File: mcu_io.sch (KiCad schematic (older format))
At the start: 6 parts

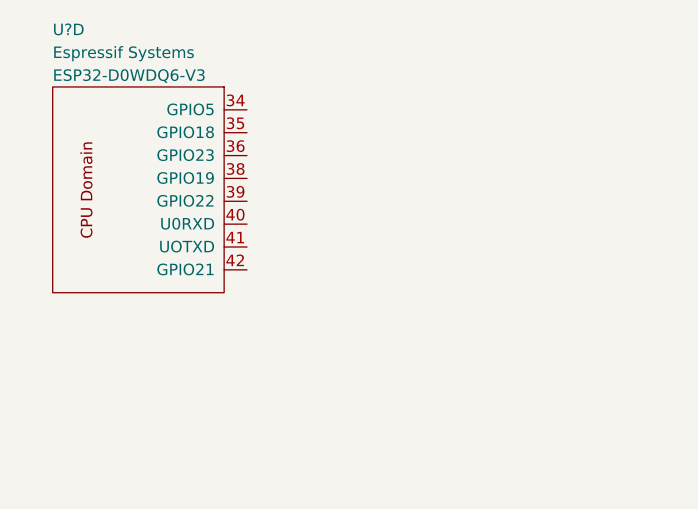
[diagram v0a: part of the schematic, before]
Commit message: Add power and boot mode LED's.
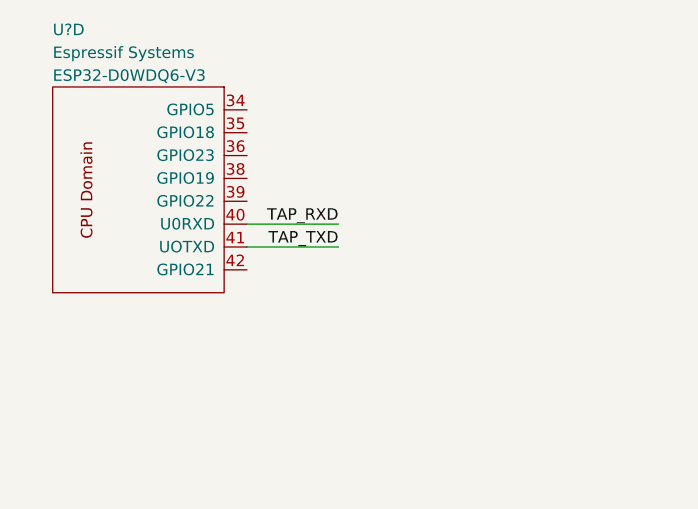
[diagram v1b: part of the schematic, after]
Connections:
- net TAP_RXD: now reaches U?.40 (U0RXD)
- net TAP_TXD: now reaches U?.41 (UOTXD)
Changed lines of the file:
@@
 	0    1    1    0
 $EndComp
+Wire Wire Line
+	2150 1900 2550 1900
+Wire Wire Line
+	2150 2000 2550 2000
+Text Label 2550 2000 2    50   ~ 0
+TAP_TXD
+Text Label 2550 1900 2    50   ~ 0
+TAP_RXD
 $EndSCHEMATC

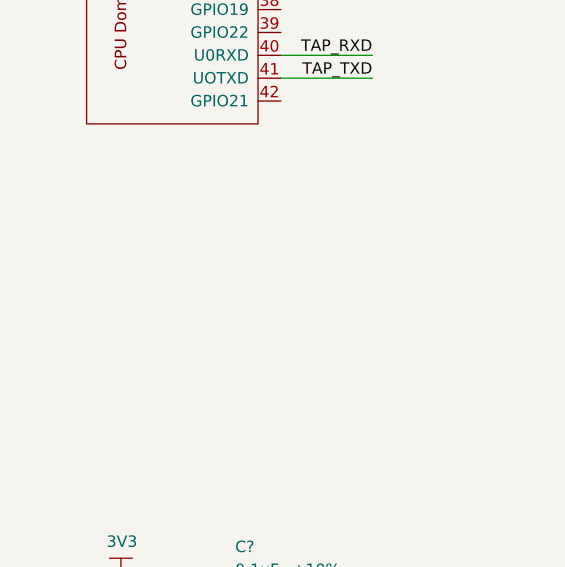
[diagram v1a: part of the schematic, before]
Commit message: Add TAP interface.
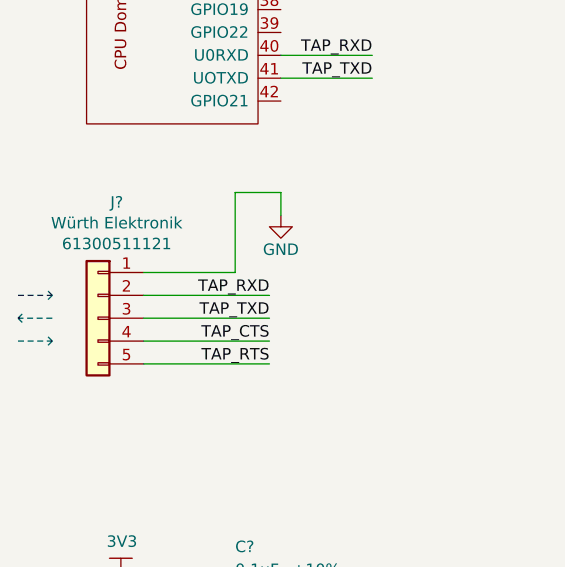
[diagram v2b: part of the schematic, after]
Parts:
- added J?: WE-61300511121, footprints:WE-61300511121_HDRV5W79P254_5X1_1270X254H854, symbol gz_Rectangular-Connectors-Headers-Male-Pins:WE-61300511121
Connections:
- net GND: now also J?.1 (Pin_1)
- net TAP_RXD: now also J?.2 (Pin_2)
- net TAP_TXD: now also J?.3 (Pin_3)
- new net TAP_CTS: J?.4 (Pin_4)
- new net TAP_RTS: J?.5 (Pin_5)
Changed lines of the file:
@@
 Text Label 2550 1900 2    50   ~ 0
 TAP_RXD
+$Comp
+L gz_Rectangular-Connectors-Headers-Male-Pins:WE-61300511121 J?
+U 1 1 604FF7D2
+P 1350 3050
+F 0 "J?" H 1432 3557 50  0000 C CNN
+F 1 "WE-61300511121" H 1850 3900 50  0001 L CNN
+F 2 "footprints:WE-61300511121_HDRV5W79P254_5X1_1270X254H854" H 1850 4000 50  0001 L CNN
+F 3 "${DATASHEETS}/WE-6130xx11121.pdf" H 2150 2900 50  0001 L CNN
+F 4 "Digikey" H 1850 3800 50  0001 L CNN "Vendor"
+F 5 "732-5318-ND" H 2150 3800 50  0001 L CNN "Vendor_PN"
+F 6 "Würth Elektronik" H 1432 3466 50  0000 C CNN "Manufacturer"
+F 7 "61300511121" H 1432 3375 50  0000 C CNN "MPN"
+F 8 "Connectors, Interconnects" H 1850 3700 50  0001 L CNN "Category"
+F 9 "Rectangular Connectors - Headers, Male Pins" H 1850 3600 50  0001 L CNN "Family"
+F 10 "Yes" H 1350 3400 50  0001 L CNN "Fit"
+	1    1350 3050
+	1    0    0    -1
+$EndComp
+Wire Wire Line
+	1550 2850 1950 2850
+Wire Wire Line
+	1550 2950 2100 2950
+Wire Wire Line
+	1550 3050 2100 3050
+Wire Wire Line
+	1550 3150 2100 3150
+Wire Wire Line
+	1550 3250 2100 3250
+$Comp
+L gz_Power-Symbols:GND #PWR?
+U 1 1 605045A7
+P 2150 2600
+AR Path="/60330427/605045A7" Ref="#PWR?"  Part="1"
+AR Path="/606CDE66/605045A7" Ref="#PWR?"  Part="1"
+F 0 "#PWR?" H 2150 2350 50  0001 C CNN
+F 1 "GND" H 2150 2450 50  0000 C CNN
+F 2 "" H 2150 2600 50  0001 C CNN
+F 3 "" H 2150 2600 50  0001 C CNN
+	1    2150 2600
+	1    0    0    -1
+$EndComp
+Wire Wire Line
+	2150 2600 2150 2500
+Wire Wire Line
+	2150 2500 1950 2500
+Wire Wire Line
+	1950 2500 1950 2850
+Text Label 2100 2950 2    50   ~ 0
+TAP_RXD
+Text Label 2100 3050 2    50   ~ 0
+TAP_TXD
+Text Label 2100 3150 2    50   ~ 0
+TAP_CTS
+Text Label 2100 3250 2    50   ~ 0
+TAP_RTS
+Wire Notes Line style solid
+	1000 2950 1150 2950
+Wire Notes Line style solid
+	1150 2950 1125 2925
+Wire Notes Line style solid
+	1150 2950 1125 2975
+Wire Notes Line style solid
+	1150 3050 1000 3050
+Wire Notes Line style solid
+	1000 3050 1025 3075
+Wire Notes Line style solid
+	1000 3050 1025 3025
+Wire Notes Line style solid
+	1000 3150 1150 3150
+Wire Notes Line style solid
+	1150 3150 1125 3125
+Wire Notes Line style solid
+	1150 3150 1125 3175
 $EndSCHEMATC

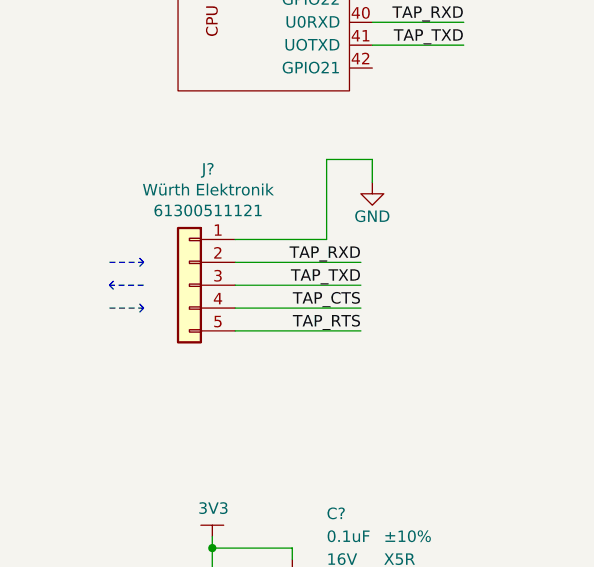
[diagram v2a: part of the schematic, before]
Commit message: Add flow control to TAP to auto-flash ESP32.
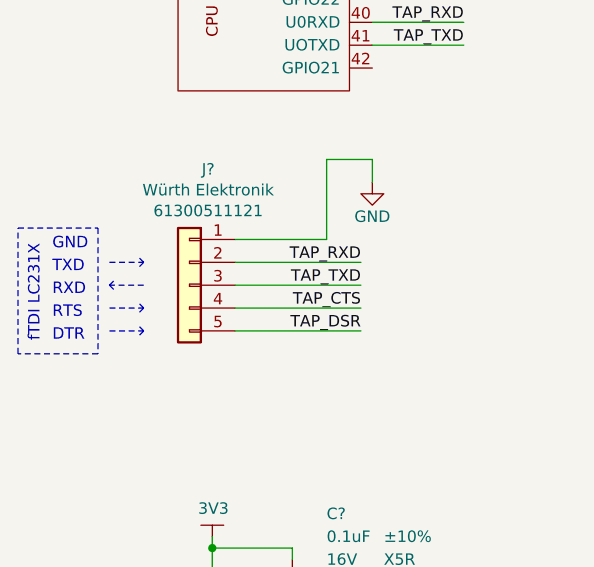
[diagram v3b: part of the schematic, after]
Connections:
- net TAP_RTS renamed TAP_DSR
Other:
- note added: "DTR"
- note added: "GND"
- note added: "RTS"
- note added: "RXD"
- note added: "TXD"
- note added: "fTDI LC231X"
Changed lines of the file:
@@
 TAP_CTS
 Text Label 2100 3250 2    50   ~ 0
-TAP_RTS
+TAP_DSR
 Wire Notes Line style solid
 	1000 2950 1150 2950
@@
 Wire Notes Line style solid
 	1150 3150 1125 3175
+Wire Notes Line style solid
+	1000 3250 1150 3250
+Wire Notes Line style solid
+	1150 3250 1125 3225
+Wire Notes Line style solid
+	1150 3250 1125 3275
+Text Notes 750  3000 0    50   ~ 0
+TXD
+Text Notes 750  3100 0    50   ~ 0
+RXD
+Text Notes 750  3200 0    50   ~ 0
+RTS
+Text Notes 750  3300 0    50   ~ 0
+DTR
+Text Notes 750  2900 0    50   ~ 0
+GND
+Text Notes 700  3300 1    50   ~ 0
+fTDI LC231X
+Wire Notes Line
+	600  2800 950  2800
+Wire Notes Line
+	950  2800 950  3350
+Wire Notes Line
+	950  3350 600  3350
+Wire Notes Line
+	600  3350 600  2800
 $EndSCHEMATC

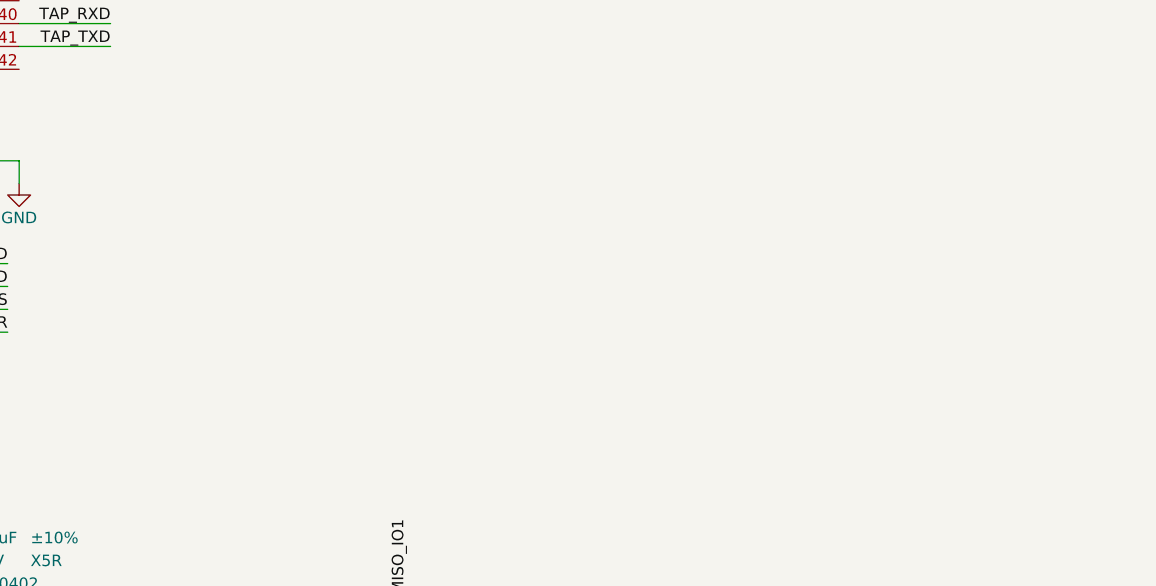
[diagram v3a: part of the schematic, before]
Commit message: Add auto-flash circuit to prevent DTR == 1 && RTS == 1 condition to keep ESP32 in reset.
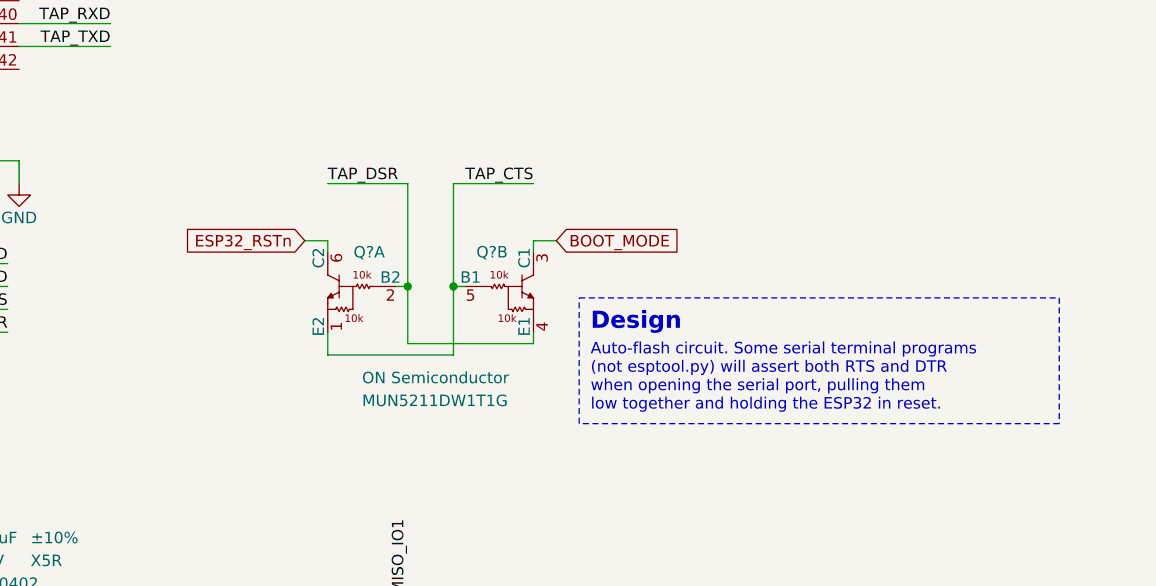
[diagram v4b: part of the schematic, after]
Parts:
- added Q? (x2): ON-Semi_MUN5211DW1T1G, footprints:ON-Semi-MUN5211DW1T1G_SOT23-6P65_210X110L36X20L, symbol gz_Transistors-Bipolar-BJT-Arrays-Pre-Biased:ON-Semi_MUN5211DW1T1G
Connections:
- net TAP_CTS: now also Q?.1 (E2), Q?.5 (B1)
- net TAP_DSR: now also Q?.2 (B2), Q?.4 (E1)
- new net BOOT_MODE: Q?.3 (C1)
- new net ESP32_RSTn: Q?.6 (C2)
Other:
- note added: "Auto-flash circuit. Some serial terminal programs\n(not esptool.py) will assert both RTS and DTR \nwhen opening the serial port, pulling them\nlow together and holding the ESP32 in reset."
- note added: "Design"
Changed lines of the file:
@@
 Text Notes 700  3300 1    50   ~ 0
 fTDI LC231X
+Wire Notes Line style solid
+	600  2800 950  2800
+Wire Notes Line style solid
+	950  2800 950  3350
+Wire Notes Line style solid
+	950  3350 600  3350
+Wire Notes Line style solid
+	600  3350 600  2800
+$Comp
+L gz_Transistors-Bipolar-BJT-Arrays-Pre-Biased:ON-Semi_MUN5211DW1T1G Q?
+U 1 1 6050B898
+P 3550 3050
+F 0 "Q?" H 3350 3200 50  0000 L CNN
+F 1 "ON-Semi_MUN5211DW1T1G" H 3900 4500 50  0001 L CNN
+F 2 "footprints:ON-Semi-MUN5211DW1T1G_SOT23-6P65_210X110L36X20L" H 3900 4600 50  0001 L CNN
+F 3 "${DATASHEETS}/ON-Semi_MUN5211DW1T1G.pdf" H 3900 3500 50  0001 L CNN
+F 4 "Digikey" H 3900 4400 50  0001 L CNN "Vendor"
+F 5 "MUN5211DW1T1GOSCT-ND" H 4300 4400 50  0001 L CNN "Vendor_PN"
+F 6 "ON Semiconductor" H 3700 3000 50  0001 L CNN "Manufacturer"
+F 7 "MUN5211DW1T1G" H 3750 2900 50  0001 L CNN "MPN"
+F 8 "Discrete Semiconductor Products" H 3900 4300 50  0001 L CNN "Category"
+F 9 "Transistors - Bipolar (BJT) - Arrays, Pre-Biased" H 5300 4300 50  0001 L CNN "Family"
+F 10 "Yes" H 3850 3050 50  0001 L CNN "Fit"
+F 11 "SOT-363" H 3900 4200 50  0001 L CNN "Package"
+	1    3550 3050
+	-1   0    0    -1
+$EndComp
+$Comp
+L gz_Transistors-Bipolar-BJT-Arrays-Pre-Biased:ON-Semi_MUN5211DW1T1G Q?
+U 2 1 6050C9A5
+P 4350 3050
+F 0 "Q?" H 4150 3200 50  0000 L CNN
+F 1 "ON-Semi_MUN5211DW1T1G" H 4700 4500 50  0001 L CNN
+F 2 "footprints:ON-Semi-MUN5211DW1T1G_SOT23-6P65_210X110L36X20L" H 4700 4600 50  0001 L CNN
+F 3 "${DATASHEETS}/ON-Semi_MUN5211DW1T1G.pdf" H 4700 3500 50  0001 L CNN
+F 4 "Digikey" H 4700 4400 50  0001 L CNN "Vendor"
+F 5 "MUN5211DW1T1GOSCT-ND" H 5100 4400 50  0001 L CNN "Vendor_PN"
+F 6 "ON Semiconductor" H 3650 2650 50  0000 L CNN "Manufacturer"
+F 7 "MUN5211DW1T1G" H 3650 2550 50  0000 L CNN "MPN"
+F 8 "Discrete Semiconductor Products" H 4700 4300 50  0001 L CNN "Category"
+F 9 "Transistors - Bipolar (BJT) - Arrays, Pre-Biased" H 6100 4300 50  0001 L CNN "Family"
+F 10 "Yes" H 4650 3050 50  0001 L CNN "Fit"
+F 11 "SOT-363" H 4700 4200 50  0001 L CNN "Package"
+	2    4350 3050
+	1    0    0    -1
+$EndComp
+Wire Wire Line
+	3800 3050 3850 3050
+Wire Wire Line
+	3850 3050 3850 3300
+Wire Wire Line
+	3850 3300 4400 3300
+Wire Wire Line
+	4400 3300 4400 3250
+Wire Wire Line
+	4100 3050 4050 3050
+Wire Wire Line
+	4050 3050 4050 3350
+Wire Wire Line
+	4050 3350 3500 3350
+Wire Wire Line
+	3500 3350 3500 3250
+Connection ~ 3850 3050
+Wire Wire Line
+	4050 3050 4050 2600
+Connection ~ 4050 3050
+Text Label 3500 2600 0    50   ~ 0
+TAP_DSR
+Wire Wire Line
+	3850 2600 3850 3050
+Text Label 4400 2600 2    50   ~ 0
+TAP_CTS
+Wire Wire Line
+	3500 2900 3500 2850
+Text GLabel 3400 2850 0    50   Input ~ 0
+ESP32_RSTn
+Text GLabel 4500 2850 2    50   Input ~ 0
+BOOT_MODE
+Wire Wire Line
+	3400 2850 3500 2850
+Wire Wire Line
+	4400 2850 4400 2900
+Wire Wire Line
+	4400 2850 4500 2850
+Wire Wire Line
+	4050 2600 4400 2600
+Wire Wire Line
+	3850 2600 3500 2600
 Wire Notes Line
-	600  2800 950  2800
+	6700 3100 6700 3650
 Wire Notes Line
-	950  2800 950  3350
+	6700 3650 4600 3650
 Wire Notes Line
-	950  3350 600  3350
+	4600 3650 4600 3100
+Text Notes 4650 3250 0    75   ~ 15
+Design
+Text Notes 4650 3600 0    50   ~ 0
+Auto-flash circuit. Some serial terminal programs\n(not esptool.py) will assert both RTS and DTR \nwhen opening the serial port, pulling them\nlow together and holding the ESP32 in reset.
 Wire Notes Line
-	600  3350 600  2800
+	4600 3100 6700 3100
 $EndSCHEMATC

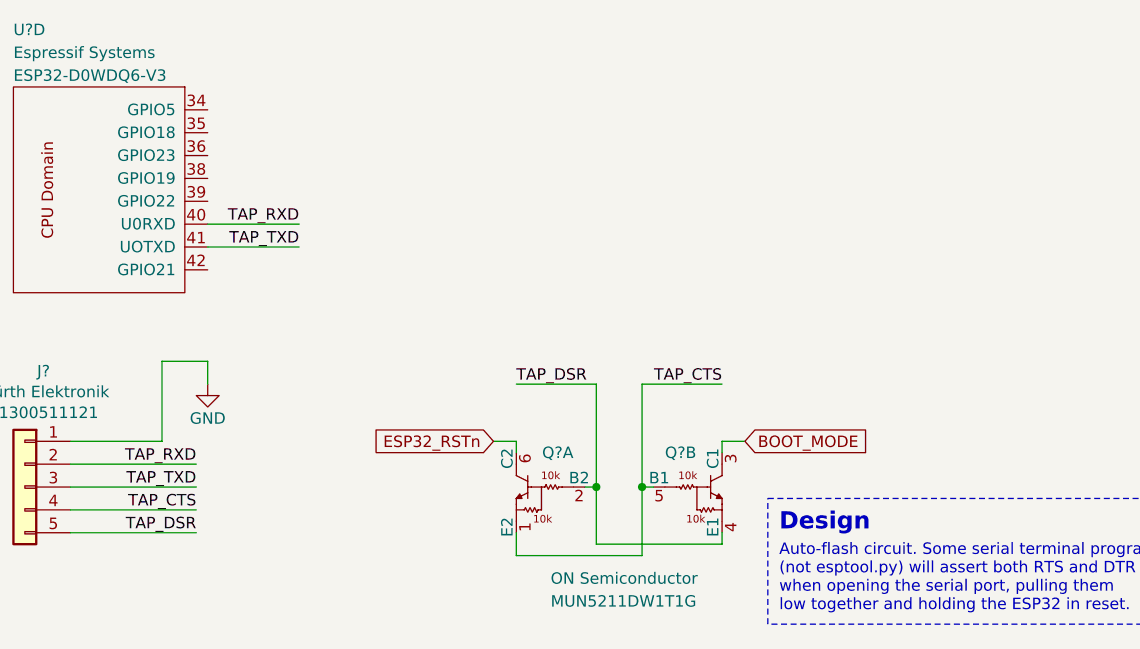
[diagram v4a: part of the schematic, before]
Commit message: Add TAP pull-ups; NF R to bypass auto-flash NPN network.
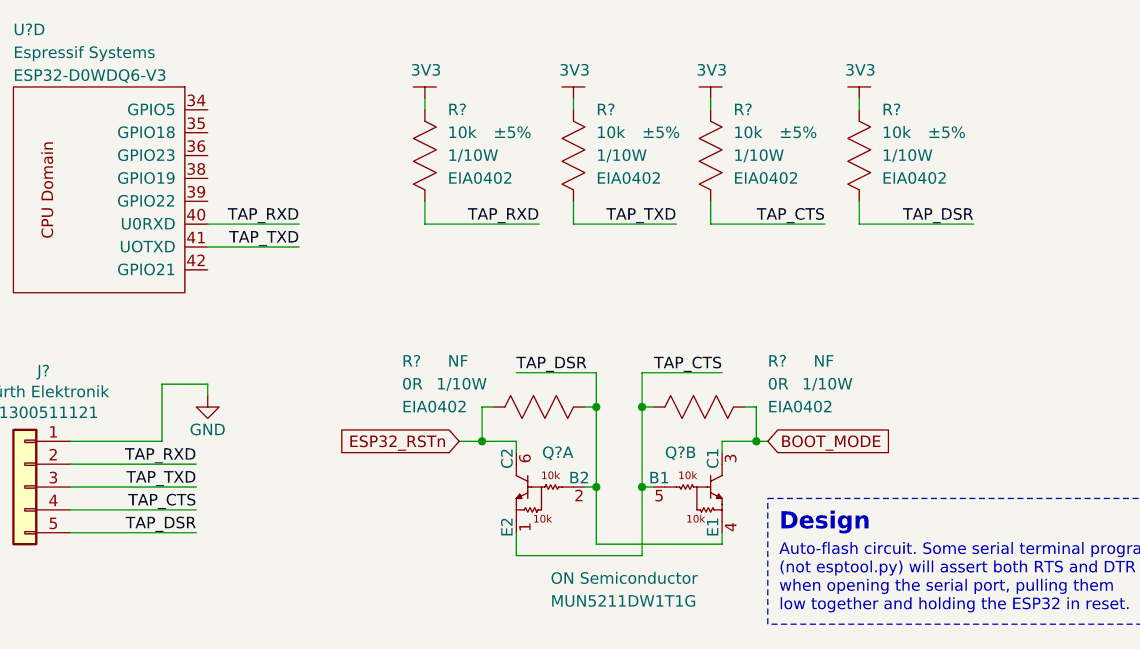
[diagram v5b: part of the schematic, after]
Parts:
- added R? (x6): RES-EIA0402, footprints_generic:RESC100X50X40L25NN, symbol gz_Chip-Resistors-Surface-Mount:RES-EIA0402
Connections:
- net +3V3: now also R?.1, R?.1, R?.1, R?.1
- net BOOT_MODE: now also R?.2
- net ESP32_RSTn: now also R?.1
- net TAP_CTS: now also R?.1, R?.2
- net TAP_DSR: now also R?.2, R?.2
- net TAP_RXD: now also R?.2
- net TAP_TXD: now also R?.2

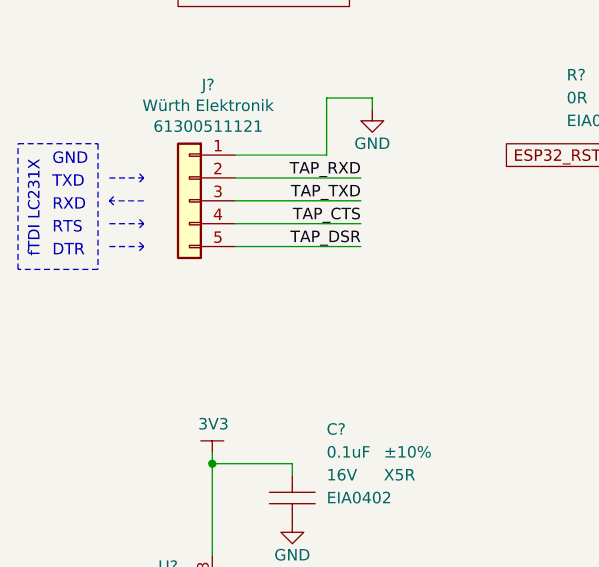
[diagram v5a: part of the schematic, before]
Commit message: Add TAP layout note; move ESP32 boot mode and reset button to I/O sheet.
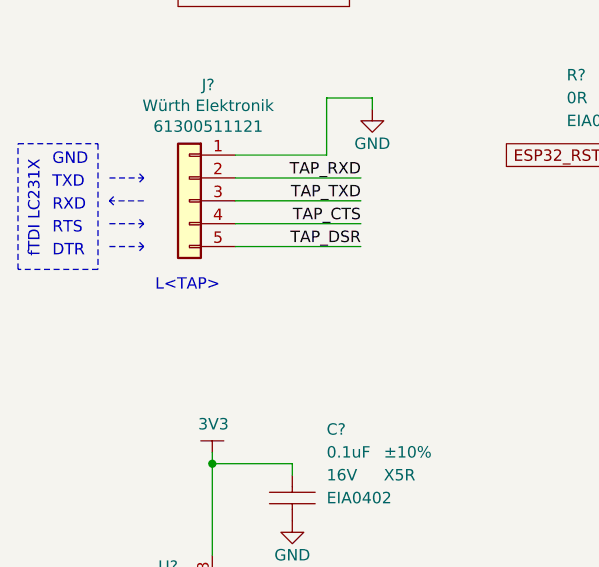
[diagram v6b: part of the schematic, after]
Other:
- note added: "L<TAP>"
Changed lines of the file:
@@
 Text Label 5500 1900 2    50   ~ 0
 TAP_DSR
+Text Notes 1200 3450 0    50   ~ 0
+L<TAP>
 $EndSCHEMATC
